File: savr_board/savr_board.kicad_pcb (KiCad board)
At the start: 6 copper layers, 0 parts

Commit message: Added footprints for fpga, ddr, and sata. Did the minimum amount of wiring to see whether it's feasible to put those on a 50x50mm JLCPCB cheapo board. Looks pretty bleak with thru-hole SATA connectors.
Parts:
- added U1: XC7Z030-CLG485, savr_board:BGA-484_22x22_19.0x19.0mm, F.Cu at (125.0, 113.0)
- added U2: DDR3_256Mx16, savr_board:BGA-96_9x16_9.0x13.5mm, F.Cu at (114.0, 131.0)
- added U3: DDR3_256Mx16, savr_board:BGA-96_9x16_9.0x13.5mm, F.Cu at (114.0, 142.0)

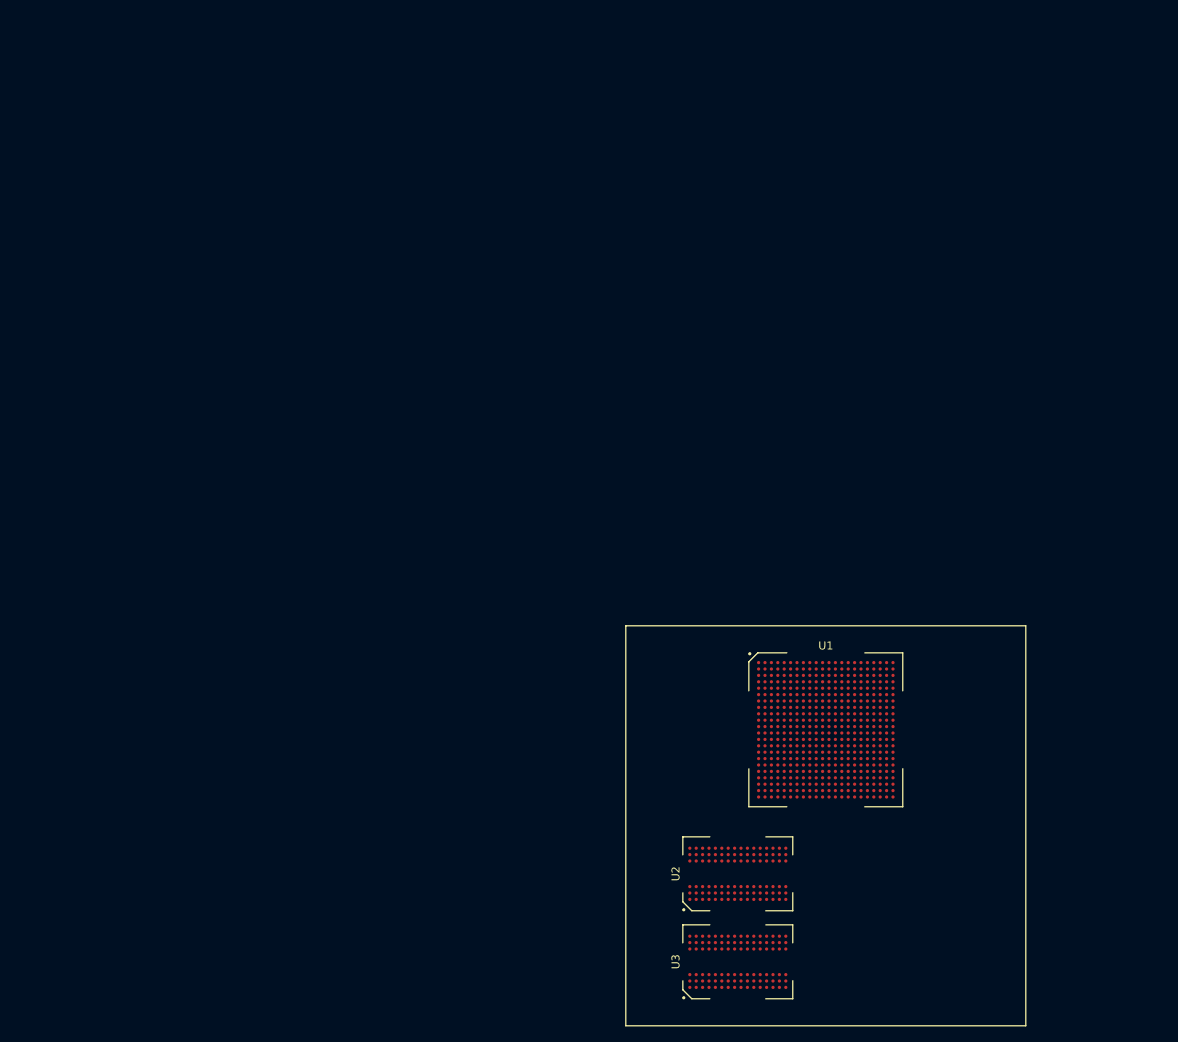
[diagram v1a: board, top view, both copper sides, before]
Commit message: Escape routing for the first 5 rows, not paying special attention to differentials
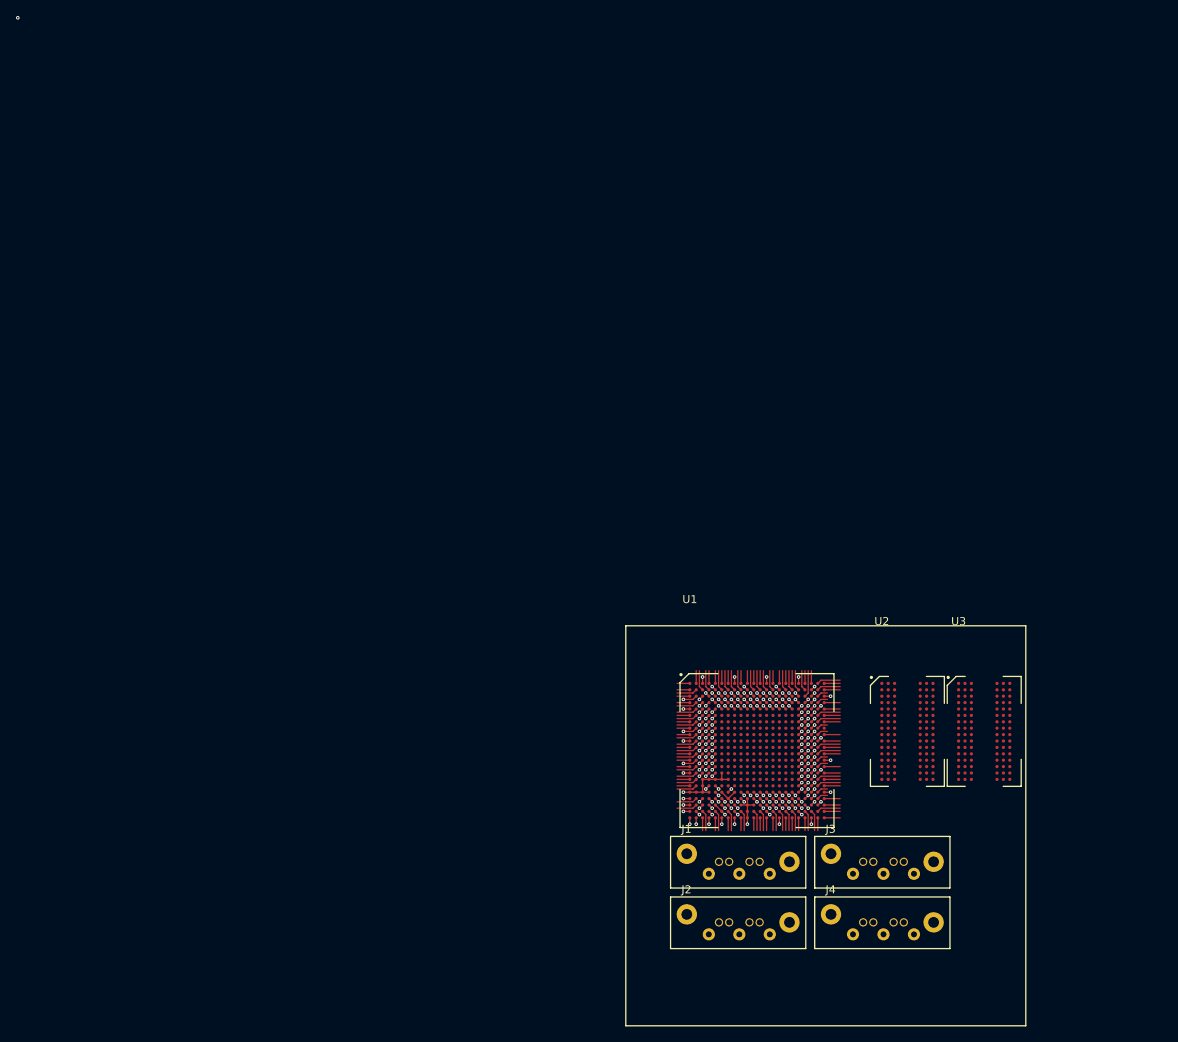
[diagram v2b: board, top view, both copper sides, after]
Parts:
- added J1: SATA-7, savr_board:SATA-7, F.Cu at (118.0, 131.0)
- added J2: SATA-7, savr_board:SATA-7, F.Cu at (118.0, 138.6)
- added J3: SATA-7, savr_board:SATA-7, F.Cu at (136.0, 131.0)
- added J4: SATA-7, savr_board:SATA-7, F.Cu at (136.0, 138.6)
- moved U3 44.4 mm to (141.6, 107.2), turned to 0 degrees
- moved U2 29.8 mm to (132.0, 107.2), turned to 0 degrees
- moved U1 18.0 mm to (108.0, 107.2)
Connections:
- net Net-(U1-PadB18) renamed /POR
- net Net-(U1-PadC14) renamed /SRST
- net Net-(U1-PadF15) renamed /MVR
- net Net-(U1-PadF16) renamed /CLK
- net Net-(U1-PadG14) renamed /BAT
- net Net-(U1-PadG9) renamed /JT3
- net Net-(U1-PadH10) renamed /JT4
- net Net-(U1-PadH11) renamed /JT1
- net Net-(U1-PadH9) renamed /JT2
- net Net-(U1-PadK11) renamed /X2
- net Net-(U1-PadK12) renamed /X1
- net Net-(U1-PadL11) renamed /X5
- net Net-(U1-PadL12) renamed /X3
- net Net-(U1-PadM11) renamed /X4
- net Net-(U1-PadM12) renamed /X6
- net Net-(U1-PadM16) renamed /DVRN
- net Net-(U1-PadN11) renamed /X7
- net Net-(U1-PadN12) renamed /X8
- net Net-(U1-PadN16) renamed /DVRP
- net Net-(U1-PadT10) renamed /PR3
- net Net-(U1-PadT8) renamed /PR2
- net Net-(U1-PadT9) renamed /PR4
- net Net-(U1-PadU5) renamed /MCLK1P
- net Net-(U1-PadU7) renamed /MVREF
- net Net-(U1-PadU9) renamed /MCLK0P
- net Net-(U1-PadV10) renamed /PR1
- net Net-(U1-PadV5) renamed /MCLK1N
- net Net-(U1-PadV7) renamed /MCAL
- net Net-(U1-PadV9) renamed /MCLK0N
- U1 pad A13: Net-(U1-PadA13) -> /VCC
- U1 pad A18: Net-(U1-PadA18) -> GND
- U1 pad A3: Net-(U1-PadA3) -> /VCC
- U1 pad A8: Net-(U1-PadA8) -> GND
- U1 pad AA1: Net-(U1-PadAA1) -> GND
- U1 pad AA10: Net-(U1-PadAA10) -> GND
- U1 pad AA13: Net-(U1-PadAA13) -> /VCC
- U1 pad AA18: Net-(U1-PadAA18) -> GND
- U1 pad AA2: Net-(U1-PadAA2) -> /VCC
- U1 pad AA21: Net-(U1-PadAA21) -> /DM3
- U1 pad AA22: Net-(U1-PadAA22) -> /DQ26
- U1 pad AA4: Net-(U1-PadAA4) -> /VCC
- U1 pad AA6: Net-(U1-PadAA6) -> GND
- U1 pad AA8: Net-(U1-PadAA8) -> /VCC
- U1 pad AB1: Net-(U1-PadAB1) -> /VCC
- U1 pad AB10: Net-(U1-PadAB10) -> GND
- U1 pad AB15: Net-(U1-PadAB15) -> GND
- U1 pad AB2: Net-(U1-PadAB2) -> GND
- U1 pad AB20: Net-(U1-PadAB20) -> /VCC
- U1 pad AB4: Net-(U1-PadAB4) -> GND
- U1 pad AB6: Net-(U1-PadAB6) -> /VCC
- U1 pad AB8: Net-(U1-PadAB8) -> GND
- U1 pad B10: Net-(U1-PadB10) -> /VCC
- U1 pad B15: Net-(U1-PadB15) -> GND
- U1 pad B20: Net-(U1-PadB20) -> /VCC
- U1 pad B21: Net-(U1-PadB21) -> /DQ2
- U1 pad B22: Net-(U1-PadB22) -> /DM0
- U1 pad B5: Net-(U1-PadB5) -> GND
- U1 pad C12: Net-(U1-PadC12) -> GND
- U1 pad C17: Net-(U1-PadC17) -> /VCC
- U1 pad C2: Net-(U1-PadC2) -> GND
- U1 pad C20: Net-(U1-PadC20) -> /DQ1
- U1 pad C21: Net-(U1-PadC21) -> /DQS0P
- U1 pad C22: Net-(U1-PadC22) -> GND
- U1 pad C7: Net-(U1-PadC7) -> /VCC
- U1 pad D14: Net-(U1-PadD14) -> /VCC
- U1 pad D19: Net-(U1-PadD19) -> GND
- U1 pad D20: Net-(U1-PadD20) -> /DQ3
- U1 pad D21: Net-(U1-PadD21) -> /DQS0N
- U1 pad D22: Net-(U1-PadD22) -> /DQ0
- U1 pad D4: Net-(U1-PadD4) -> /VCC
- U1 pad D9: Net-(U1-PadD9) -> GND
- U1 pad E1: Net-(U1-PadE1) -> /VCC
- U1 pad E11: Net-(U1-PadE11) -> /VCC
- U1 pad E16: Net-(U1-PadE16) -> GND
- U1 pad E20: Net-(U1-PadE20) -> /DQ4
- U1 pad E21: Net-(U1-PadE21) -> /VCC
- U1 pad E22: Net-(U1-PadE22) -> /DQ5
- U1 pad E6: Net-(U1-PadE6) -> GND
- U1 pad F13: Net-(U1-PadF13) -> GND
- U1 pad F18: Net-(U1-PadF18) -> /VCC
- U1 pad F19: Net-(U1-PadF19) -> /A13
- U1 pad F20: Net-(U1-PadF20) -> /DDR_RST
- U1 pad F21: Net-(U1-PadF21) -> /DQ6
- U1 pad F22: Net-(U1-PadF22) -> /DQ7
- U1 pad F3: Net-(U1-PadF3) -> GND
- U1 pad F8: Net-(U1-PadF8) -> /VCC
- U1 pad G10: Net-(U1-PadG10) -> GND
- U1 pad G12: Net-(U1-PadG12) -> GND
- U1 pad G13: Net-(U1-PadG13) -> /VCC
- U1 pad G15: Net-(U1-PadG15) -> /VCC
- U1 pad G18: Net-(U1-PadG18) -> /A11
- U1 pad G19: Net-(U1-PadG19) -> /A14
- U1 pad G20: Net-(U1-PadG20) -> GND
- U1 pad G21: Net-(U1-PadG21) -> /DQ8
- U1 pad G22: Net-(U1-PadG22) -> /DQ9
- U1 pad G5: Net-(U1-PadG5) -> /VCC
- U1 pad H12: Net-(U1-PadH12) -> /VCC
- U1 pad H13: Net-(U1-PadH13) -> GND
- U1 pad H14: Net-(U1-PadH14) -> /VCC
- U1 pad H15: Net-(U1-PadH15) -> GND
- U1 pad H16: Net-(U1-PadH16) -> /DDR_VREF
- U1 pad H17: Net-(U1-PadH17) -> GND
- U1 pad H18: Net-(U1-PadH18) -> /A9
- U1 pad H19: Net-(U1-PadH19) -> /A12
- U1 pad H2: Net-(U1-PadH2) -> /VCC
- U1 pad H20: Net-(U1-PadH20) -> /DM1
- U1 pad H21: Net-(U1-PadH21) -> /DQS1P
- U1 pad H22: Net-(U1-PadH22) -> /VCC
- U1 pad H7: Net-(U1-PadH7) -> GND
- U1 pad J10: Net-(U1-PadJ10) -> GND
- U1 pad J11: Net-(U1-PadJ11) -> /VCC
- U1 pad J12: Net-(U1-PadJ12) -> GND
- U1 pad J13: Net-(U1-PadJ13) -> /VCC
- U1 pad J14: Net-(U1-PadJ14) -> GND
- U1 pad J15: Net-(U1-PadJ15) -> /VCC
- U1 pad J16: Net-(U1-PadJ16) -> /A6
- U1 pad J17: Net-(U1-PadJ17) -> /A7
- U1 pad J18: Net-(U1-PadJ18) -> /A8
- U1 pad J19: Net-(U1-PadJ19) -> /VCC
- U1 pad J20: Net-(U1-PadJ20) -> /A10
- U1 pad J21: Net-(U1-PadJ21) -> /DQS1N
- U1 pad J22: Net-(U1-PadJ22) -> /DQ14
- U1 pad J4: Net-(U1-PadJ4) -> GND
- U1 pad J9: Net-(U1-PadJ9) -> /VCC
- U1 pad K1: Net-(U1-PadK1) -> GND
- U1 pad K10: Net-(U1-PadK10) -> /VCC
- U1 pad K13: Net-(U1-PadK13) -> GND
- U1 pad K14: Net-(U1-PadK14) -> /VCC
- U1 pad K15: Net-(U1-PadK15) -> GND
- U1 pad K16: Net-(U1-PadK16) -> /VCC
- U1 pad K17: Net-(U1-PadK17) -> /A4
- U1 pad K18: Net-(U1-PadK18) -> /A5
- U1 pad K19: Net-(U1-PadK19) -> /A2
- U1 pad K20: Net-(U1-PadK20) -> /DQ15
- U1 pad K21: Net-(U1-PadK21) -> GND
- U1 pad K22: Net-(U1-PadK22) -> /DQ13
- U1 pad K6: Net-(U1-PadK6) -> /VCC
- U1 pad K9: Net-(U1-PadK9) -> GND
- U1 pad L10: Net-(U1-PadL10) -> GND
- U1 pad L13: Net-(U1-PadL13) -> /VCC
- U1 pad L14: Net-(U1-PadL14) -> GND
- U1 pad L15: Net-(U1-PadL15) -> /VCC
- U1 pad L16: Net-(U1-PadL16) -> /BA0
- U1 pad L17: Net-(U1-PadL17) -> /BA1
- U1 pad L18: Net-(U1-PadL18) -> GND
- U1 pad L19: Net-(U1-PadL19) -> /A3
- U1 pad L20: Net-(U1-PadL20) -> /DQ12
- U1 pad L21: Net-(U1-PadL21) -> /DQ11
- U1 pad L22: Net-(U1-PadL22) -> /DQ10
- U1 pad L3: Net-(U1-PadL3) -> /VCC
- U1 pad L8: Net-(U1-PadL8) -> GND
- U1 pad L9: Net-(U1-PadL9) -> /VCC
- U1 pad M10: Net-(U1-PadM10) -> /VCC
- U1 pad M13: Net-(U1-PadM13) -> GND
- U1 pad M14: Net-(U1-PadM14) -> /VCC
- U1 pad M15: Net-(U1-PadM15) -> GND
- U1 pad M17: Net-(U1-PadM17) -> /BA2
- U1 pad M18: Net-(U1-PadM18) -> /A1
- U1 pad M19: Net-(U1-PadM19) -> /A0
- U1 pad M20: Net-(U1-PadM20) -> /VCC
- U1 pad M21: Net-(U1-PadM21) -> /DQ22
- U1 pad M22: Net-(U1-PadM22) -> /DQ16
- U1 pad M5: Net-(U1-PadM5) -> GND
- U1 pad M9: Net-(U1-PadM9) -> GND
- U1 pad N10: Net-(U1-PadN10) -> GND
- U1 pad N13: Net-(U1-PadN13) -> /VCC
- U1 pad N14: Net-(U1-PadN14) -> GND
- U1 pad N15: Net-(U1-PadN15) -> /VCC
- U1 pad N17: Net-(U1-PadN17) -> /VCC
- U1 pad N18: Net-(U1-PadN18) -> /DDR_CKN
- U1 pad N19: Net-(U1-PadN19) -> /DDR_CKP
- U1 pad N2: Net-(U1-PadN2) -> GND
- U1 pad N20: Net-(U1-PadN20) -> /DQ18
- U1 pad N21: Net-(U1-PadN21) -> /DQS2P
- U1 pad N22: Net-(U1-PadN22) -> GND
- U1 pad N7: Net-(U1-PadN7) -> /VCC
- U1 pad N9: Net-(U1-PadN9) -> /VCC
- U1 pad P10: Net-(U1-PadP10) -> /VCC
- U1 pad P11: Net-(U1-PadP11) -> GND
- U1 pad P12: Net-(U1-PadP12) -> /VCC
- U1 pad P13: Net-(U1-PadP13) -> GND
- U1 pad P14: Net-(U1-PadP14) -> /VCC
- U1 pad P15: Net-(U1-PadP15) -> GND
- U1 pad P16: Net-(U1-PadP16) -> /DDR_VREF
- U1 pad P17: Net-(U1-PadP17) -> /DDR_CS
- U1 pad P18: Net-(U1-PadP18) -> /DDR_ODT
- U1 pad P19: Net-(U1-PadP19) -> GND
- U1 pad P20: Net-(U1-PadP20) -> /CAS
- U1 pad P21: Net-(U1-PadP21) -> /DQS2N
- U1 pad P22: Net-(U1-PadP22) -> /DM2
- U1 pad P4: Net-(U1-PadP4) -> /VCC
- U1 pad P9: Net-(U1-PadP9) -> GND
- U1 pad R1: Net-(U1-PadR1) -> /VCC
- U1 pad R10: Net-(U1-PadR10) -> GND
- U1 pad R11: Net-(U1-PadR11) -> /VCC
- U1 pad R12: Net-(U1-PadR12) -> GND
- U1 pad R13: Net-(U1-PadR13) -> /VCC
- U1 pad R14: Net-(U1-PadR14) -> GND
- U1 pad R15: Net-(U1-PadR15) -> /VCC
- U1 pad R16: Net-(U1-PadR16) -> GND
- U1 pad R18: Net-(U1-PadR18) -> /RAS
- U1 pad R19: Net-(U1-PadR19) -> /WE
- U1 pad R20: Net-(U1-PadR20) -> /DQ20
- U1 pad R21: Net-(U1-PadR21) -> /VCC
- U1 pad R22: Net-(U1-PadR22) -> /DQ23
- U1 pad R6: Net-(U1-PadR6) -> GND
- U1 pad R9: Net-(U1-PadR9) -> /VCC
- U1 pad T11: Net-(U1-PadT11) -> /VCC
- U1 pad T12: Net-(U1-PadT12) -> /VCC
- U1 pad T13: Net-(U1-PadT13) -> GND
- U1 pad T14: Net-(U1-PadT14) -> /VCC
- U1 pad T15: Net-(U1-PadT15) -> /VCC
- U1 pad T18: Net-(U1-PadT18) -> /VCC
- U1 pad T19: Net-(U1-PadT19) -> /DDR_CKE
- U1 pad T20: Net-(U1-PadT20) -> /DQ17
- U1 pad T21: Net-(U1-PadT21) -> /DQ21
- U1 pad T22: Net-(U1-PadT22) -> /DQ19
- U1 pad T3: Net-(U1-PadT3) -> GND
- U1 pad T4: Net-(U1-PadT4) -> GND
- U1 pad T5: Net-(U1-PadT5) -> GND
- U1 pad T6: Net-(U1-PadT6) -> GND
- U1 pad T7: Net-(U1-PadT7) -> GND
- U1 pad U10: Net-(U1-PadU10) -> GND
- U1 pad U15: Net-(U1-PadU15) -> /VCC
- U1 pad U20: Net-(U1-PadU20) -> GND
- U1 pad U21: Net-(U1-PadU21) -> /DQ27
- U1 pad U22: Net-(U1-PadU22) -> /DQ25
- U1 pad U3: Net-(U1-PadU3) -> GND
- U1 pad U4: Net-(U1-PadU4) -> /VCC
- U1 pad U6: Net-(U1-PadU6) -> /VCC
- U1 pad U8: Net-(U1-PadU8) -> /VCC
- U1 pad V1: Net-(U1-PadV1) -> GND
- U1 pad V12: Net-(U1-PadV12) -> /VCC
- U1 pad V17: Net-(U1-PadV17) -> GND
- U1 pad V2: Net-(U1-PadV2) -> GND
- U1 pad V20: Net-(U1-PadV20) -> /DQ30
- U1 pad V21: Net-(U1-PadV21) -> /DQS3P
- U1 pad V22: Net-(U1-PadV22) -> /VCC
- U1 pad V3: Net-(U1-PadV3) -> GND
- U1 pad V4: Net-(U1-PadV4) -> GND
- U1 pad V6: Net-(U1-PadV6) -> GND
- U1 pad V8: Net-(U1-PadV8) -> GND
- U1 pad W1: Net-(U1-PadW1) -> GND
- U1 pad W10: Net-(U1-PadW10) -> GND
- U1 pad W14: Net-(U1-PadW14) -> GND
- U1 pad W19: Net-(U1-PadW19) -> /VCC
- U1 pad W20: Net-(U1-PadW20) -> /DQ29
- U1 pad W21: Net-(U1-PadW21) -> /DQS3N
- U1 pad W22: Net-(U1-PadW22) -> /DQ28
- U1 pad W3: Net-(U1-PadW3) -> /VCC
- U1 pad W5: Net-(U1-PadW5) -> /VCC
- U1 pad W7: Net-(U1-PadW7) -> GND
- U1 pad W9: Net-(U1-PadW9) -> /VCC
- U1 pad Y1: Net-(U1-PadY1) -> GND
- U1 pad Y10: Net-(U1-PadY10) -> GND
- U1 pad Y11: Net-(U1-PadY11) -> GND
- U1 pad Y16: Net-(U1-PadY16) -> /VCC
- U1 pad Y20: Net-(U1-PadY20) -> /DQ24
- U1 pad Y21: Net-(U1-PadY21) -> GND
- U1 pad Y22: Net-(U1-PadY22) -> /DQ31
- U1 pad Y3: Net-(U1-PadY3) -> GND
- U1 pad Y5: Net-(U1-PadY5) -> GND
- U1 pad Y7: Net-(U1-PadY7) -> /VCC
- U1 pad Y9: Net-(U1-PadY9) -> GND
- U2 pad A2: Net-(U2-PadA2) -> /DQ13
- U2 pad A3: Net-(U2-PadA3) -> /DQ15
- U2 pad A7: Net-(U2-PadA7) -> /DQ12
- U2 pad B7: Net-(U2-PadB7) -> /DQS1N
- U2 pad B8: Net-(U2-PadB8) -> /DQ14
- U2 pad C2: Net-(U2-PadC2) -> /DQ11
- U2 pad C3: Net-(U2-PadC3) -> /DQ9
- U2 pad C7: Net-(U2-PadC7) -> /DQS1P
- U2 pad C8: Net-(U2-PadC8) -> /DQ10
- U2 pad D3: Net-(U2-PadD3) -> /DM1
- U2 pad D7: Net-(U2-PadD7) -> /DQ8
- U2 pad E3: Net-(U2-PadE3) -> /DQ0
- U2 pad E7: Net-(U2-PadE7) -> /DM0
- U2 pad F2: Net-(U2-PadF2) -> /DQ2
- U2 pad F3: Net-(U2-PadF3) -> /DQS0P
- U2 pad F7: Net-(U2-PadF7) -> /DQ1
- U2 pad F8: Net-(U2-PadF8) -> /DQ3
- U2 pad G2: Net-(U2-PadG2) -> /DQ6
- U2 pad G3: Net-(U2-PadG3) -> /DQS0N
- U2 pad H1: Net-(U2-PadH1) -> /DDR_VREF
- U2 pad H3: Net-(U2-PadH3) -> /DQ4
- U2 pad H7: Net-(U2-PadH7) -> /DQ7
- U2 pad H8: Net-(U2-PadH8) -> /DQ5
- U2 pad J3: Net-(U2-PadJ3) -> /RAS
- U2 pad J7: Net-(U2-PadJ7) -> /DDR_CKP
- U2 pad K1: Net-(U2-PadK1) -> /DDR_ODT
- U2 pad K3: Net-(U2-PadK3) -> /CAS
- U2 pad K7: Net-(U2-PadK7) -> /DDR_CKN
- U2 pad K9: Net-(U2-PadK9) -> /DDR_CKE
- U2 pad L2: Net-(U2-PadL2) -> /DDR_CS
- U2 pad L3: Net-(U2-PadL3) -> /WE
- U2 pad L7: Net-(U2-PadL7) -> /A10
- U2 pad M2: Net-(U2-PadM2) -> /BA0
- U2 pad M3: Net-(U2-PadM3) -> /BA2
- U2 pad M8: Net-(U2-PadM8) -> /DDR_VREF
- U2 pad N2: Net-(U2-PadN2) -> /A3
- U2 pad N3: Net-(U2-PadN3) -> /A0
- U2 pad N7: Net-(U2-PadN7) -> /A12
- U2 pad N8: Net-(U2-PadN8) -> /BA1
- U2 pad P2: Net-(U2-PadP2) -> /A5
- U2 pad P3: Net-(U2-PadP3) -> /A2
- U2 pad P7: Net-(U2-PadP7) -> /A1
- U2 pad P8: Net-(U2-PadP8) -> /A4
- U2 pad R2: Net-(U2-PadR2) -> /A7
- U2 pad R3: Net-(U2-PadR3) -> /A9
- U2 pad R7: Net-(U2-PadR7) -> /A11
- U2 pad R8: Net-(U2-PadR8) -> /A6
- U2 pad T2: Net-(U2-PadT2) -> /DDR_RST
- U2 pad T3: Net-(U2-PadT3) -> /A13
- U2 pad T7: Net-(U2-PadT7) -> /A14
- U2 pad T8: Net-(U2-PadT8) -> /A8
- U3 pad A2: Net-(U3-PadA2) -> /DQ29
- U3 pad A3: Net-(U3-PadA3) -> /DQ31
- U3 pad A7: Net-(U3-PadA7) -> /DQ28
- U3 pad B7: Net-(U3-PadB7) -> /DQS3N
- U3 pad B8: Net-(U3-PadB8) -> /DQ30
- U3 pad C2: Net-(U3-PadC2) -> /DQ27
- U3 pad C3: Net-(U3-PadC3) -> /DQ25
- U3 pad C7: Net-(U3-PadC7) -> /DQS3P
- U3 pad C8: Net-(U3-PadC8) -> /DQ26
- U3 pad D3: Net-(U3-PadD3) -> /DM3
- U3 pad D7: Net-(U3-PadD7) -> /DQ24
- U3 pad E3: Net-(U3-PadE3) -> /DQ16
- U3 pad E7: Net-(U3-PadE7) -> /DM2
- U3 pad F2: Net-(U3-PadF2) -> /DQ18
- U3 pad F3: Net-(U3-PadF3) -> /DQS2P
- U3 pad F7: Net-(U3-PadF7) -> /DQ17
- U3 pad F8: Net-(U3-PadF8) -> /DQ19
- U3 pad G2: Net-(U3-PadG2) -> /DQ22
- U3 pad G3: Net-(U3-PadG3) -> /DQS2N
- U3 pad H1: Net-(U3-PadH1) -> /DDR_VREF
- U3 pad H3: Net-(U3-PadH3) -> /DQ20
- U3 pad H7: Net-(U3-PadH7) -> /DQ23
- U3 pad H8: Net-(U3-PadH8) -> /DQ21
- U3 pad J3: Net-(U3-PadJ3) -> /RAS
- U3 pad J7: Net-(U3-PadJ7) -> /DDR_CKP
- U3 pad K1: Net-(U3-PadK1) -> /DDR_ODT
- U3 pad K3: Net-(U3-PadK3) -> /CAS
- U3 pad K7: Net-(U3-PadK7) -> /DDR_CKN
- U3 pad K9: Net-(U3-PadK9) -> /DDR_CKE
- U3 pad L2: Net-(U3-PadL2) -> /DDR_CS
- U3 pad L3: Net-(U3-PadL3) -> /WE
- U3 pad L7: Net-(U3-PadL7) -> /A10
- U3 pad M2: Net-(U3-PadM2) -> /BA0
- U3 pad M3: Net-(U3-PadM3) -> /BA2
- U3 pad M8: Net-(U3-PadM8) -> /DDR_VREF
- U3 pad N2: Net-(U3-PadN2) -> /A3
- U3 pad N3: Net-(U3-PadN3) -> /A0
- U3 pad N7: Net-(U3-PadN7) -> /A12
- U3 pad N8: Net-(U3-PadN8) -> /BA1
- U3 pad P2: Net-(U3-PadP2) -> /A5
- U3 pad P3: Net-(U3-PadP3) -> /A2
- U3 pad P7: Net-(U3-PadP7) -> /A1
- U3 pad P8: Net-(U3-PadP8) -> /A4
- U3 pad R2: Net-(U3-PadR2) -> /A7
- U3 pad R3: Net-(U3-PadR3) -> /A9
- U3 pad R7: Net-(U3-PadR7) -> /A11
- U3 pad R8: Net-(U3-PadR8) -> /A6
- U3 pad T2: Net-(U3-PadT2) -> /DDR_RST
- U3 pad T3: Net-(U3-PadT3) -> /A13
- U3 pad T7: Net-(U3-PadT7) -> /A14
- U3 pad T8: Net-(U3-PadT8) -> /A8
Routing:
- net GND: track 0.00 -> 42.6 mm, vias 0 -> 38
- net /VCC: track 0.00 -> 24.0 mm, vias 0 -> 37
- net /MCLK1P: track 0.00 -> 7.39 mm, vias 0 -> 1
- net /MCLK1N: track 0.00 -> 6.97 mm, vias 0 -> 1
- net /MCAL: track 0.00 -> 6.90 mm, vias 0 -> 1
- net Net-(U1-PadE4): track 0.00 -> 6.59 mm, vias 0 -> 1
- net Net-(U1-PadE19): track 0.00 -> 6.59 mm, vias 0 -> 1
- net Net-(U1-PadV19): track 0.00 -> 6.59 mm, vias 0 -> 1
- net Net-(U1-PadP5): track 0.00 -> 6.50 mm, vias 0 -> 1
- net Net-(U1-PadJ5): track 0.00 -> 6.50 mm, vias 0 -> 1
- net /DDR_ODT: track 0.00 -> 6.50 mm, vias 0 -> 1
- net Net-(U1-PadE18): track 0.00 -> 6.33 mm, vias 0 -> 1
- net /RAS: track 0.00 -> 6.33 mm, vias 0 -> 1
- net /A5: track 0.00 -> 6.33 mm, vias 0 -> 1
- net Net-(U1-PadR5): track 0.00 -> 6.33 mm, vias 0 -> 1
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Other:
- net class Default: clearance 0.127 -> 0.1016; trace_width 0.1524 -> 0.1016; via_dia 0.762 -> 0.45; via_drill 0.5588 -> 0.2
- rule pad_to_mask_clearance: 0.0508 -> 0.1016
- rule trace_clearance: 0.127 -> 0.1016
- rule via_min_drill: 0.200152 -> 0.2
- rule via_min_size: 0.45212 -> 0.45

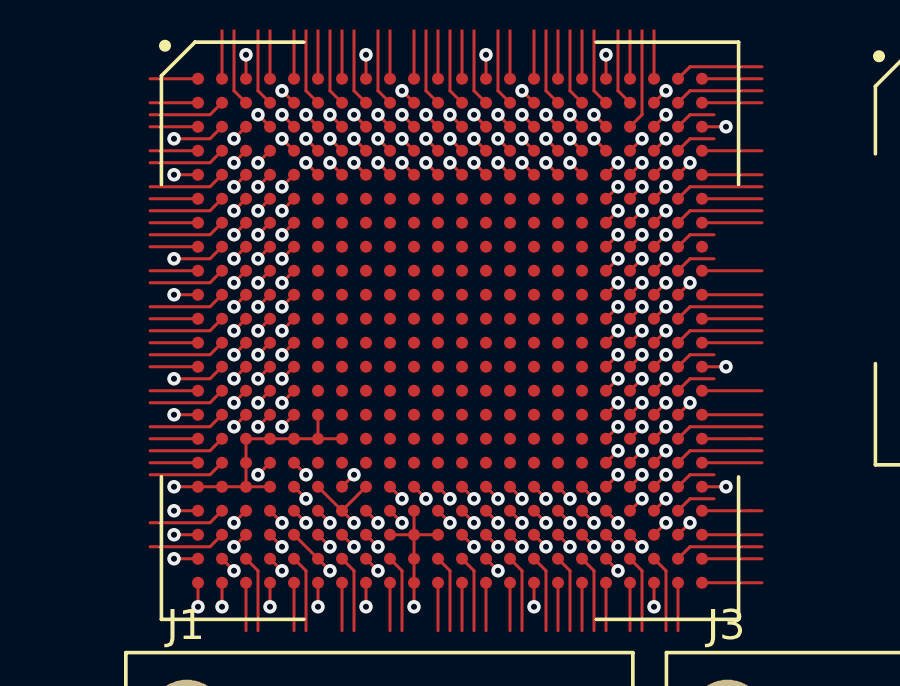
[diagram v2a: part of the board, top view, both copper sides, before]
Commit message: I did it! Complete escape with 4 signal layers. There are a few places where I might have to rip something up: the VRP / VRN nets require resistors to ground and vcc, so those must have bottom layer space.
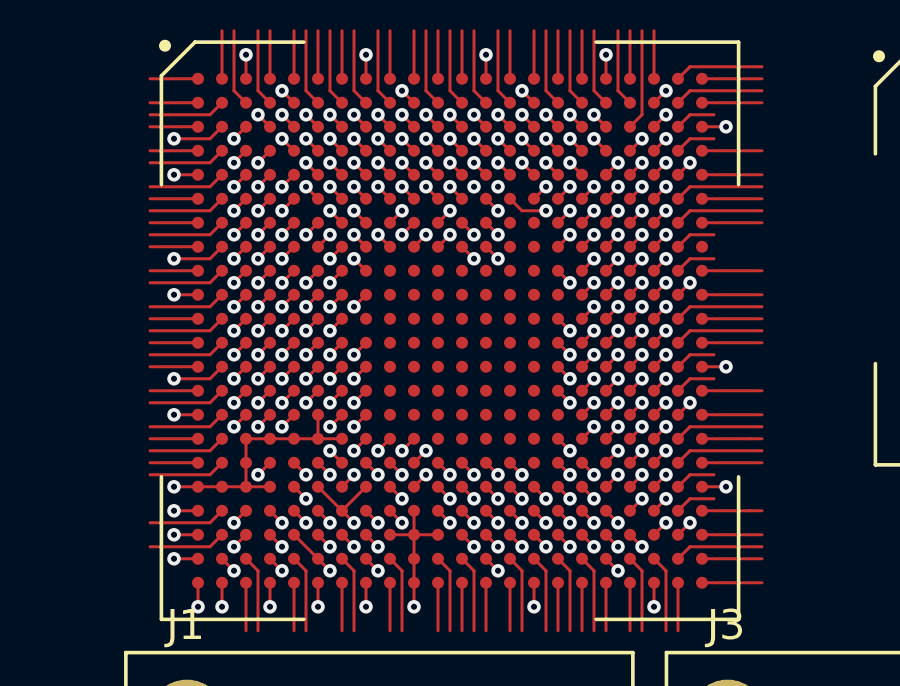
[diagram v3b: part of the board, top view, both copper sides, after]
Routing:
- net /DDR_VREF: track 0.00 -> 17.5 mm, vias 0 -> 2
- net /JT1: track 0.00 -> 14.0 mm, vias 0 -> 1
- net /JT4: track 0.00 -> 13.9 mm, vias 0 -> 1
- net /JT2: track 0.00 -> 13.8 mm, vias 0 -> 2
- net Net-(U1-PadM8): track 0.00 -> 13.3 mm, vias 0 -> 1
- net /JT3: track 0.00 -> 13.3 mm, vias 0 -> 1
- net Net-(U1-PadM7): track 0.00 -> 13.0 mm, vias 0 -> 1
- net Net-(U1-PadH8): track 0.00 -> 12.4 mm, vias 0 -> 1
- net Net-(U1-PadN8): track 0.00 -> 11.6 mm, vias 0 -> 1
- net Net-(U1-PadP8): track 0.00 -> 11.4 mm, vias 0 -> 1
- net Net-(U1-PadJ8): track 0.00 -> 11.3 mm, vias 0 -> 1
- net Net-(U1-PadF14): track 0.00 -> 10.9 mm, vias 0 -> 1
- net Net-(U1-PadG8): track 0.00 -> 10.3 mm, vias 0 -> 1
- net Net-(U1-PadP7): track 0.00 -> 9.89 mm, vias 0 -> 1
- net Net-(U1-PadP6): track 0.00 -> 9.39 mm, vias 0 -> 1
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
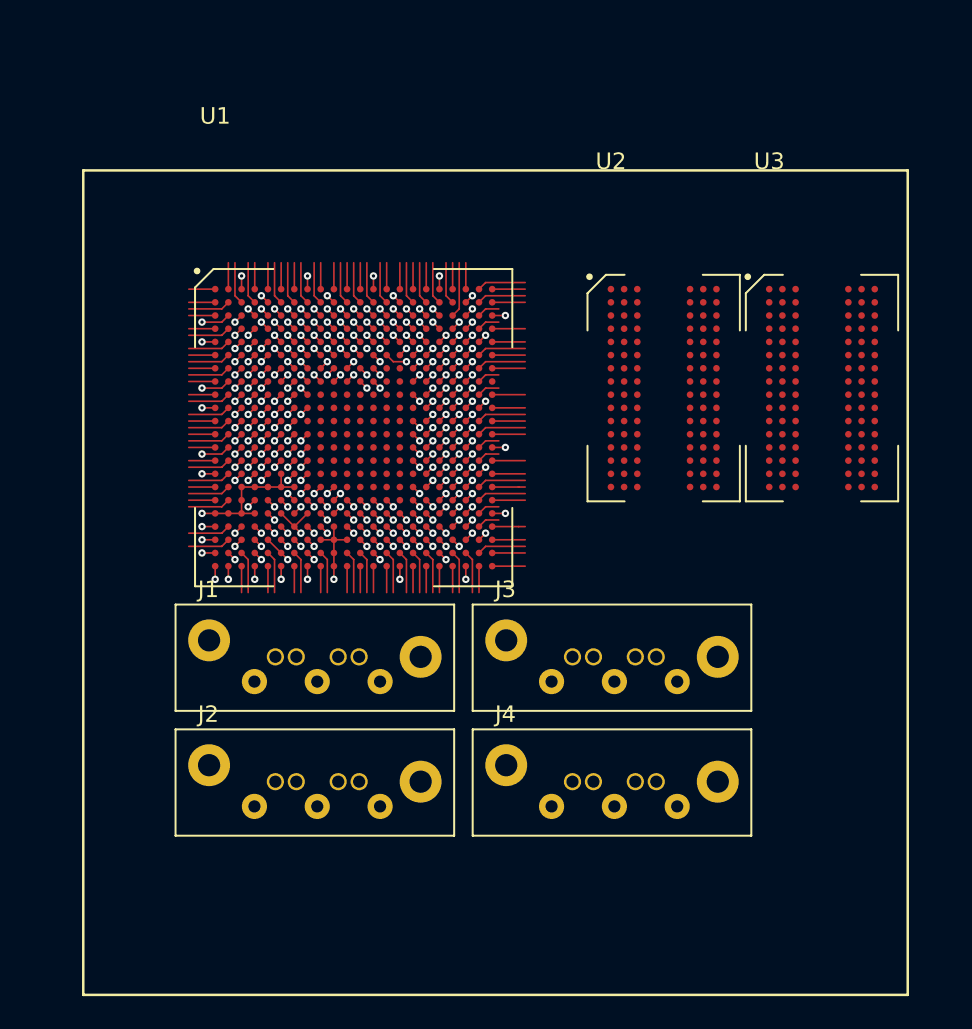
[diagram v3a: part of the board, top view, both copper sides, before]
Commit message: Feasibility test of IO connectors and SATA routing
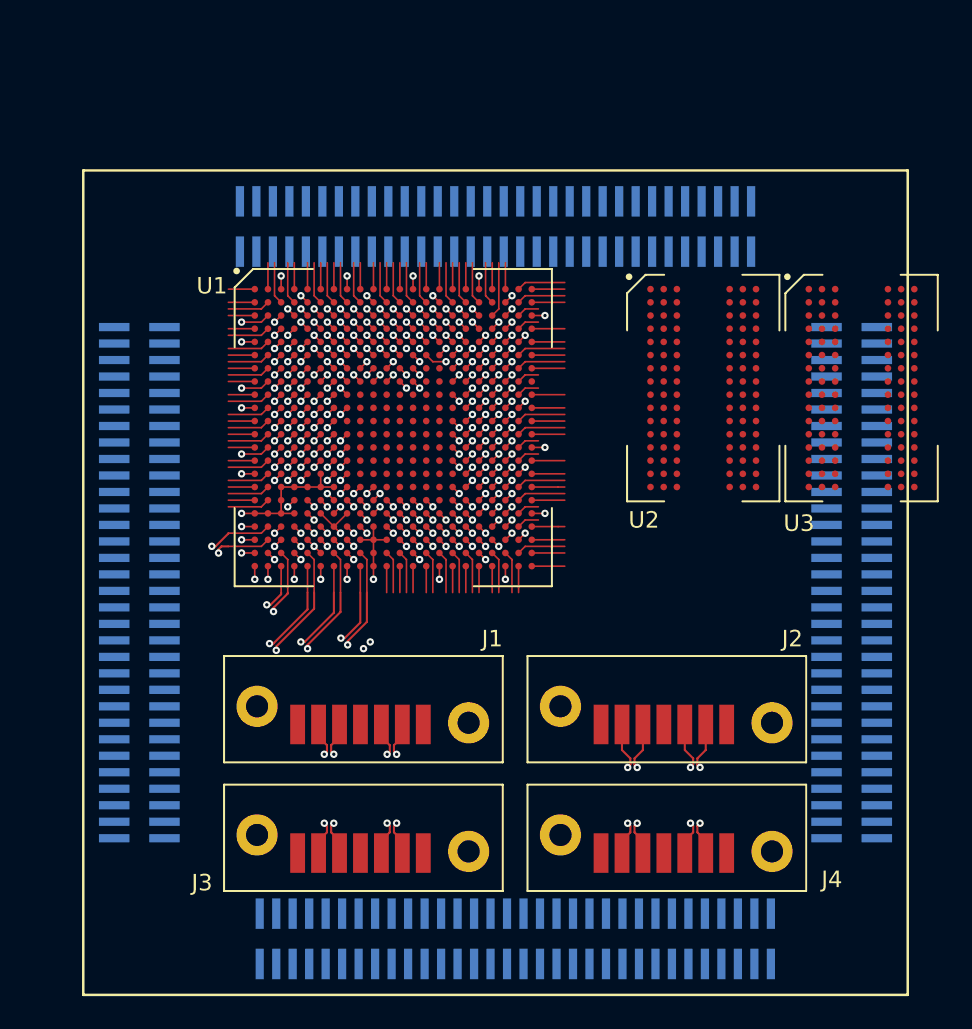
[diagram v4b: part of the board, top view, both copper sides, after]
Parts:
- added REF**: PinSocket_2x32_P1.00mm_Vertical_SMD, Connector_PinSocket_1.00mm:PinSocket_2x32_P1.00mm_Vertical_SMD, B.Cu at (125.0, 103.4)
- added REF**: PinSocket_2x32_P1.00mm_Vertical_SMD, Connector_PinSocket_1.00mm:PinSocket_2x32_P1.00mm_Vertical_SMD, B.Cu at (146.6, 125.0)
- added REF**: PinSocket_2x32_P1.00mm_Vertical_SMD, Connector_PinSocket_1.00mm:PinSocket_2x32_P1.00mm_Vertical_SMD, B.Cu at (126.2, 146.6)
- added REF**: PinSocket_2x32_P1.00mm_Vertical_SMD, Connector_PinSocket_1.00mm:PinSocket_2x32_P1.00mm_Vertical_SMD, B.Cu at (103.4, 125.0)
- J1, J2, J3, J4: footprint savr_board:SATA-7 -> savr_board:SATA-7-SMD-vert
- moved J3 25.3 mm to (113.0, 141.4), turned to 180 degrees
- moved J2 14.3 mm to (131.4, 133.6), turned to 180 degrees
- moved J1 5.64 mm to (113.0, 133.6), turned to 180 degrees
- moved J4 5.42 mm to (131.4, 141.4), turned to 180 degrees
- moved U1 2.40 mm to (110.4, 107.2)
- moved U2 2.40 mm to (134.4, 107.2)
- moved U3 2.40 mm to (144.0, 107.2)
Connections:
- net Net-(J1-Pad2) renamed /TX0P
- net Net-(J1-Pad3) renamed /TX0N
- net Net-(J1-Pad5) renamed /RX0P
- net Net-(J1-Pad6) renamed /RX0N
- net Net-(J2-Pad2) renamed /TX1P
- net Net-(J2-Pad3) renamed /TX1N
- net Net-(J2-Pad5) renamed /RX1P
- net Net-(J2-Pad6) renamed /RX1N
- net Net-(J3-Pad2) renamed /TX2P
- net Net-(J3-Pad3) renamed /TX2N
- net Net-(J3-Pad5) renamed /RX2P
- net Net-(J3-Pad6) renamed /RX2N
- net Net-(J4-Pad2) renamed /TX3P
- net Net-(J4-Pad3) renamed /TX3N
- net Net-(J4-Pad5) renamed /RX3P
- net Net-(J4-Pad6) renamed /RX3N
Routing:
- net /TX3P: track 2.57 -> 45.2 mm, vias 0 -> 2
- net /TX3N: track 2.57 -> 44.5 mm, vias 0 -> 2
- net /RX3N: track 3.93 -> 37.1 mm, vias 1 -> 3
- net /RX3P: track 4.90 -> 37.0 mm, vias 1 -> 3
- net /RX1N: track 3.93 -> 33.1 mm, vias 1 -> 2
- net /TX1N: track 3.93 -> 32.7 mm, vias 1 -> 2
- net /RX1P: track 4.90 -> 32.8 mm, vias 1 -> 2
- net /TX1P: track 4.90 -> 32.4 mm, vias 1 -> 2
- net /TX2N: track 1.60 -> 25.6 mm, vias 0 -> 2
- net /TX2P: track 2.57 -> 25.6 mm, vias 0 -> 2
- net /RX2N: track 1.60 -> 24.3 mm, vias 0 -> 2
- net /RX2P: track 2.57 -> 24.4 mm, vias 0 -> 2
- net /RX0N: track 1.60 -> 18.7 mm, vias 0 -> 2
- net /TX0N: track 1.60 -> 17.7 mm, vias 0 -> 2
- net /RX0P: track 2.57 -> 18.5 mm, vias 0 -> 2
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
